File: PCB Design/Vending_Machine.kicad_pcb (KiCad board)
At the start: 2 copper layers, 116.6 x 143.7 mm, 178 parts, among them J1 Mains, J11 Conn_Aux, J12 Conn_Sig, J13 Conn_I2C, J14 Conn_I2C, J2 Conn_IO, J3 Conn_IO11, J31 GPIO5, J32 GPIO3, J33 GPIO2, J34 GPIO4, J35 Conn_01x15, J36 UART0, J37 Display, J38 Conn_01x15, J39 GPIO1, J4 Conn_IO12, J40 I2C, J42 Conn, J43 Conn_I2C, J46 Conn_I2C, J47 Conn_Sig, J48 I2C, SW31 EN, SW32 BOOT, U11 AMS1117-3.3, U12 SX1509BIULTRT, U13 TCA9406DC, U31 AMS1117-3.3, U32 TCA9406DC, U33 ESP32-WROOM-32UE, U41 AMS1117-3.3, U42 SX1509BIULTRT, U43 TCA9406DC

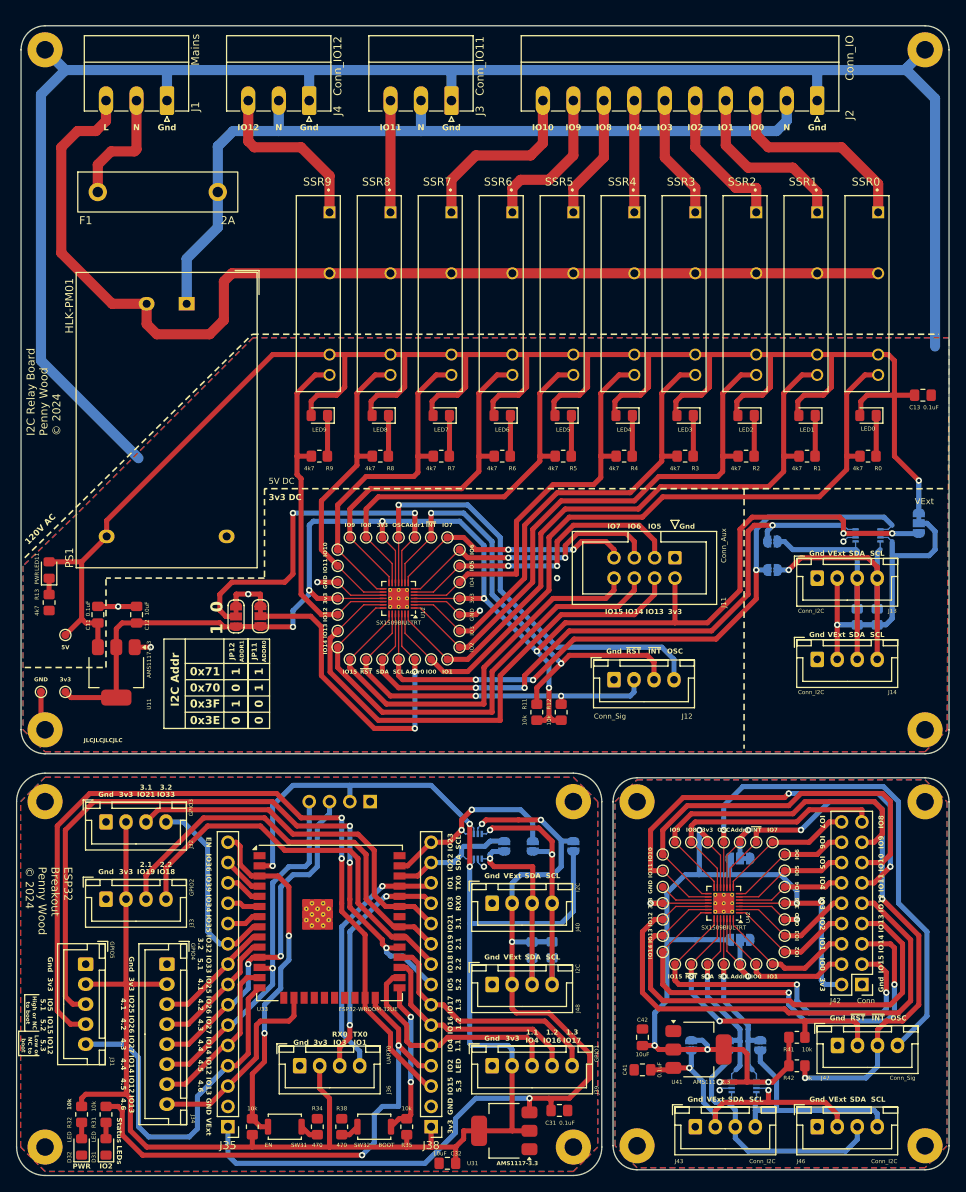
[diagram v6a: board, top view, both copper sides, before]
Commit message: Ready for production
Moved connectors to slightly overlap board edge
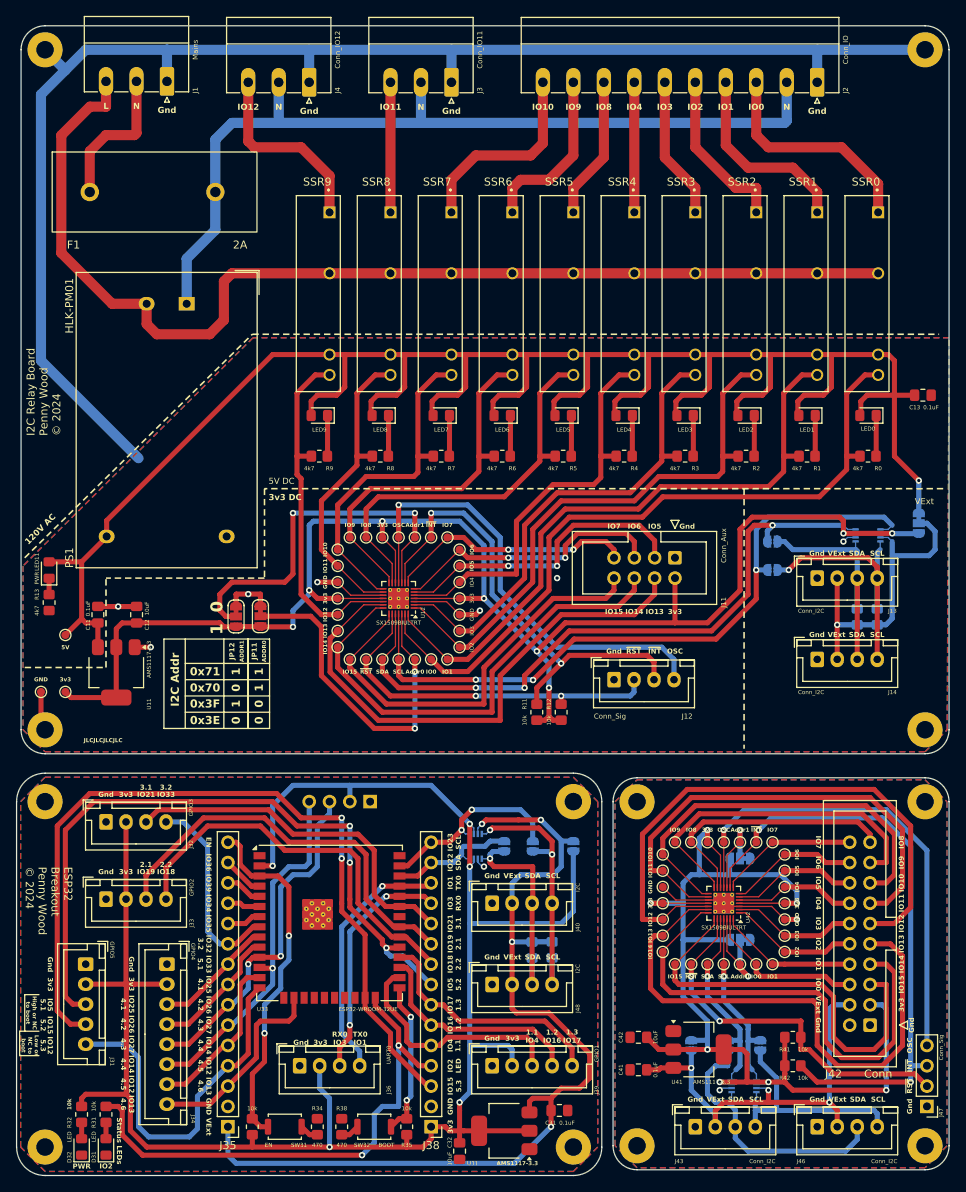
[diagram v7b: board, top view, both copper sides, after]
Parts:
- J42: footprint Connector_PinHeader_2.54mm:PinHeader_2x09_P2.54mm_Vertical -> Connector_IDC:IDC-Header_2x10_P2.54mm_Vertical
- J47: footprint Connector_JST:JST_XH_B4B-XH-A_1x04_P2.50mm_Vertical -> Connector_PinHeader_2.54mm:PinHeader_1x04_P2.54mm_Vertical
- moved J47 13.5 mm to (161.0, 182.9), turned to 180 degrees
- moved J42 5.18 mm to (153.9, 172.7)
- moved J1 2.40 mm to (66.0, 54.7)
- moved J2 2.29 mm to (147.3, 54.9)
- moved J3 2.29 mm to (101.6, 54.9)
- moved J4 2.29 mm to (83.8, 54.9)
- moved C32 2.16 mm to (102.6, 188.5), turned to -90 degrees
- moved F1 1.00 mm to (56.4, 68.6)
- moved R41 0.51 mm to (144.3, 174.2)
- moved R42 0.51 mm to (144.3, 177.8)
- moved C41 0.51 mm to (125.0, 178.3)
- moved C42 0.51 mm to (125.0, 174.2), turned to 180 degrees
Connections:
- J42 pad 10: /IO Multiplexer/IO3 -> /IO Multiplexer/IO2
- J42 pad 11: /IO Multiplexer/IO11 -> /IO Multiplexer/IO12
- J42 pad 12: /IO Multiplexer/IO4 -> /IO Multiplexer/IO3
- J42 pad 13: /IO Multiplexer/IO10 -> /IO Multiplexer/IO11
- J42 pad 14: /IO Multiplexer/IO5 -> /IO Multiplexer/IO4
- J42 pad 15: /IO Multiplexer/IO9 -> /IO Multiplexer/IO10
- J42 pad 16: /IO Multiplexer/IO6 -> /IO Multiplexer/IO5
- J42 pad 17: /IO Multiplexer/IO8 -> /IO Multiplexer/IO9
- J42 pad 18: /IO Multiplexer/IO7 -> /IO Multiplexer/IO6
- J42 pad 2: /IO Multiplexer/3v3 -> /IO Multiplexer/GND
- J42 pad 3: /IO Multiplexer/IO15 -> /IO Multiplexer/3v3
- J42 pad 4: /IO Multiplexer/IO0 -> /IO Multiplexer/VExt
- J42 pad 5: /IO Multiplexer/IO14 -> /IO Multiplexer/IO15
- J42 pad 6: /IO Multiplexer/IO1 -> /IO Multiplexer/IO0
- J42 pad 7: /IO Multiplexer/IO13 -> /IO Multiplexer/IO14
- J42 pad 8: /IO Multiplexer/IO2 -> /IO Multiplexer/IO1
- J42 pad 9: /IO Multiplexer/IO12 -> /IO Multiplexer/IO13
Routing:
- net /Relay Controller/GND: track 254.6 -> 219.6 mm
- net /IO Multiplexer/VExt: track 38.8 -> 54.5 mm, vias 2 -> 3
- net /IO Multiplexer/IO13: track 60.1 -> 70.3 mm
- net /IO Multiplexer/3v3: track 131.5 -> 140.8 mm, vias 8 -> 7
- net /IO Multiplexer/~{RST}: track 37.7 -> 47.0 mm
- net /IO Multiplexer/OSCIO: track 67.3 -> 60.1 mm
- net /Relay Controller/Neut: track 103.9 -> 109.5 mm
- net /IO Multiplexer/IO12: track 68.0 -> 73.4 mm
- net /IO Multiplexer/IO15: track 47.3 -> 52.0 mm, vias 2 -> 0
- net /IO Multiplexer/GND: track 15.8 -> 20.1 mm
- net /IO Multiplexer/IO14: track 56.4 -> 60.5 mm, vias 2 -> 0
- net Net-(J1-Pin_2): track 15.1 -> 18.3 mm
- net Net-(J4-Pin_3): track 21.6 -> 23.9 mm
- net Net-(J3-Pin_3): track 14.0 -> 16.3 mm
- net Net-(J2-Pin_7): track 14.0 -> 16.3 mm
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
